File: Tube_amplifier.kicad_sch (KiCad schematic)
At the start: 3 parts, among them U1 6N2P, U2 6P14P

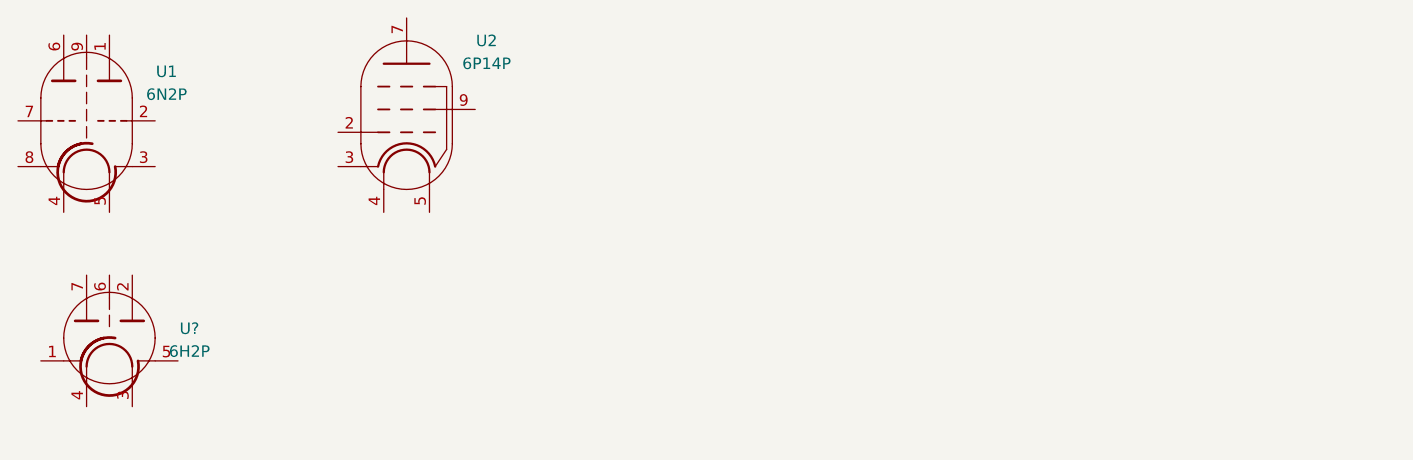
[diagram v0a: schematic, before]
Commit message: 7-pin socket 3d model added
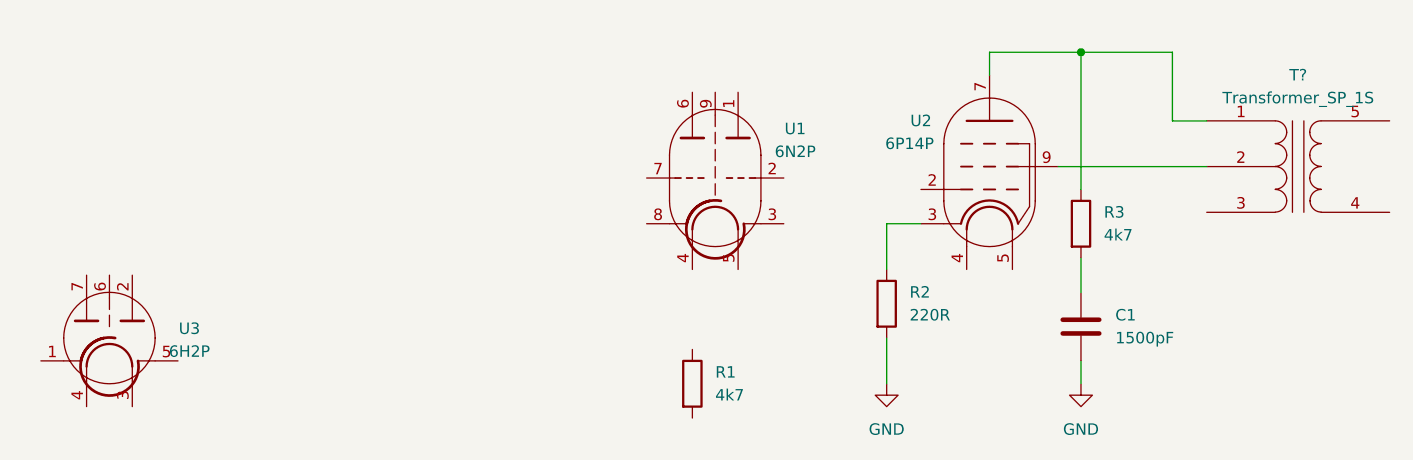
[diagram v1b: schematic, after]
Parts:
- added C1: 1500pF, Capacitor_THT:C_Rect_L7.2mm_W3.0mm_P5.00mm_FKS2_FKP2_MKS2_MKP2, symbol Device:C
- added R1: 4k7, spdf1626_lib:R_THT_025W, symbol Device:R
- added R2: 220R, spdf1626_lib:R_THT_1W, symbol Device:R
- added R3: 4k7, spdf1626_lib:R_THT_1W, symbol Device:R
- added T?: Transformer_SP_1S, symbol Device:Transformer_SP_1S
- gave numbers to parts that had none: 1
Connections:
- net at U2.3: now also R2.1
- net at U2.7: now also R3.1, T?.1 (PR1)
- net at U2.9: now also T?.2 (PM)
- new net: C1.1, R3.2
- new net GND: C1.2, R2.2
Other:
- moved on the sheet: U1, U2
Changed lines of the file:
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@@
 (kicad_sch (version 20211123) (generator eeschema)
   (paper "A4")
+  (junction (at 149.86 40.64) (diameter 0) (color 0 0 0 0)
+  )
+  (wire (pts (xy 147.32 53.34) (xy 163.83 53.34))
+    (stroke (width 0) (type default) (color 0 0 0 0))
+  )
+  (wire (pts (xy 149.86 40.64) (xy 139.7 40.64))
+    (stroke (width 0) (type default) (color 0 0 0 0))
+  )
+  (wire (pts (xy 160.02 48.26) (xy 160.02 40.64))
+    (stroke (width 0) (type default) (color 0 0 0 0))
+  )
+  (wire (pts (xy 139.7 40.64) (xy 139.7 43.18))
+    (stroke (width 0) (type default) (color 0 0 0 0))
+  )
+  (wire (pts (xy 128.27 64.77) (xy 128.27 59.69))
+    (stroke (width 0) (type default) (color 0 0 0 0))
+  )
+  (wire (pts (xy 149.86 55.88) (xy 149.86 40.64))
+    (stroke (width 0) (type default) (color 0 0 0 0))
+  )
+  (wire (pts (xy 163.83 48.26) (xy 160.02 48.26))
+    (stroke (width 0) (type default) (color 0 0 0 0))
+  )
+  (wire (pts (xy 128.27 72.39) (xy 128.27 77.47))
+    (stroke (width 0) (type default) (color 0 0 0 0))
+  )
+  (wire (pts (xy 149.86 63.5) (xy 149.86 67.31))
+    (stroke (width 0) (type default) (color 0 0 0 0))
+  )
+  (wire (pts (xy 128.27 59.69) (xy 132.08 59.69))
+    (stroke (width 0) (type default) (color 0 0 0 0))
+  )
+  (wire (pts (xy 160.02 40.64) (xy 149.86 40.64))
+    (stroke (width 0) (type default) (color 0 0 0 0))
+  )
+  (wire (pts (xy 149.86 74.93) (xy 149.86 77.47))
+    (stroke (width 0) (type default) (color 0 0 0 0))
+  )
+  (symbol (lib_id "power:GND") (at 128.27 77.47 0) (unit 1)
+    (in_bom yes) (on_board yes) (fields_autoplaced)
+    (property "Reference" "#PWR0101" (id 0) (at 128.27 83.82 0)
+      (effects (font (size 1.27 1.27)) hide)
+    )
+    (property "Value" "GND" (id 1) (at 128.27 82.55 0))
+    (property "Footprint" "" (id 2) (at 128.27 77.47 0)
+      (effects (font (size 1.27 1.27)) hide)
+    )
+    (property "Datasheet" "" (id 3) (at 128.27 77.47 0)
+      (effects (font (size 1.27 1.27)) hide)
+    )
+    (pin "1")
+  )
+  (symbol (lib_id "Device:R") (at 106.68 77.47 0) (unit 1)
+    (in_bom yes) (on_board yes) (fields_autoplaced)
+    (property "Reference" "R1" (id 0) (at 109.22 76.1999 0)
+      (effects (font (size 1.27 1.27)) (justify left))
+    )
+    (property "Value" "4k7" (id 1) (at 109.22 78.7399 0)
+      (effects (font (size 1.27 1.27)) (justify left))
+    )
+    (property "Footprint" "spdf1626_lib:R_THT_025W" (id 2) (at 104.902 77.47 90)
+      (effects (font (size 1.27 1.27)) hide)
+    )
+    (property "Datasheet" "~" (id 3) (at 106.68 77.47 0)
+      (effects (font (size 1.27 1.27)) hide)
+    )
+    (pin "1")
+    (pin "2")
+  )
+  (symbol (lib_id "Device:C") (at 149.86 71.12 0) (unit 1)
+    (in_bom yes) (on_board yes) (fields_autoplaced)
+    (property "Reference" "C1" (id 0) (at 153.67 69.8499 0)
+      (effects (font (size 1.27 1.27)) (justify left))
+    )
+    (property "Value" "1500pF" (id 1) (at 153.67 72.3899 0)
+      (effects (font (size 1.27 1.27)) (justify left))
+    )
+    (property "Footprint" "Capacitor_THT:C_Rect_L7.2mm_W3.0mm_P5.00mm_FKS2_FKP2_MKS2_MKP2" (id 2) (at 150.8252 74.93 0)
+      (effects (font (size 1.27 1.27)) hide)
+    )
+    (property "Datasheet" "~" (id 3) (at 149.86 71.12 0)
+      (effects (font (size 1.27 1.27)) hide)
+    )
+    (pin "1")
+    (pin "2")
+  )
+  (symbol (lib_id "Device:R") (at 128.27 68.58 0) (unit 1)
+    (in_bom yes) (on_board yes) (fields_autoplaced)
+    (property "Reference" "R2" (id 0) (at 130.81 67.3099 0)
+      (effects (font (size 1.27 1.27)) (justify left))
+    )
+    (property "Value" "220R" (id 1) (at 130.81 69.8499 0)
+      (effects (font (size 1.27 1.27)) (justify left))
+    )
+    (property "Footprint" "spdf1626_lib:R_THT_1W" (id 2) (at 126.492 68.58 90)
+      (effects (font (size 1.27 1.27)) hide)
+    )
+    (property "Datasheet" "~" (id 3) (at 128.27 68.58 0)
+      (effects (font (size 1.27 1.27)) hide)
+    )
+    (pin "1")
+    (pin "2")
+  )
+  (symbol (lib_id "power:GND") (at 149.86 77.47 0) (unit 1)
+    (in_bom yes) (on_board yes) (fields_autoplaced)
+    (property "Reference" "#PWR0102" (id 0) (at 149.86 83.82 0)
+      (effects (font (size 1.27 1.27)) hide)
+    )
+    (property "Value" "GND" (id 1) (at 149.86 82.55 0))
+    (property "Footprint" "" (id 2) (at 149.86 77.47 0)
+      (effects (font (size 1.27 1.27)) hide)
+    )
+    (property "Datasheet" "" (id 3) (at 149.86 77.47 0)
+      (effects (font (size 1.27 1.27)) hide)
+    )
+    (pin "1")
+  )
   (symbol (lib_id "spdf1626:6H2P") (at 41.91 72.39 0) (unit 1)
     (in_bom yes) (on_board yes) (fields_autoplaced)
-    (property "Reference" "U?" (id 0) (at 50.8 71.3486 0))
+    (property "Reference" "U3" (id 0) (at 50.8 71.3486 0))
     (property "Value" "6H2P" (id 1) (at 50.8 73.8886 0))
     (property "Footprint" "spdf1626_lib:9-pin_tube_socket" (id 2) (at 36.83 83.82 0)
@@
     (pin "7")
   )
-  (symbol (lib_id "spdf1626:6N2P") (at 39.37 48.26 0) (unit 1)
-    (in_bom yes) (on_board yes) (fields_autoplaced)
-    (property "Reference" "U1" (id 0) (at 48.26 42.7988 0))
-    (property "Value" "6N2P" (id 1) (at 48.26 45.3388 0))
-    (property "Footprint" "spdf1626_lib:9-pin_tube_socket" (id 2) (at 34.29 59.69 0)
-      (effects (font (size 1.27 1.27)) hide)
-    )
-    (property "Datasheet" "" (id 3) (at 39.37 50.8 0)
+  (symbol (lib_id "spdf1626:6N2P") (at 109.22 54.61 0) (unit 1)
+    (in_bom yes) (on_board yes) (fields_autoplaced)
+    (property "Reference" "U1" (id 0) (at 118.11 49.1488 0))
+    (property "Value" "6N2P" (id 1) (at 118.11 51.6888 0))
+    (property "Footprint" "spdf1626_lib:9-pin_tube_socket" (id 2) (at 104.14 66.04 0)
+      (effects (font (size 1.27 1.27)) hide)
+    )
+    (property "Datasheet" "" (id 3) (at 109.22 57.15 0)
       (effects (font (size 1.27 1.27)) hide)
     )
@@
     (pin "9")
   )
-  (symbol (lib_id "spdf1626:6P14P") (at 74.93 48.26 0) (unit 1)
+  (symbol (lib_id "Device:Transformer_SP_1S") (at 173.99 53.34 0) (unit 1)
+    (in_bom yes) (on_board yes) (fields_autoplaced)
+    (property "Reference" "T?" (id 0) (at 174.0027 43.18 0))
+    (property "Value" "Transformer_SP_1S" (id 1) (at 174.0027 45.72 0))
+    (property "Footprint" "" (id 2) (at 173.99 53.34 0)
+      (effects (font (size 1.27 1.27)) hide)
+    )
+    (property "Datasheet" "~" (id 3) (at 173.99 53.34 0)
+      (effects (font (size 1.27 1.27)) hide)
+    )
+    (pin "1")
+    (pin "2")
+    (pin "3")
+    (pin "4")
+    (pin "5")
+  )
+  (symbol (lib_id "spdf1626:6P14P") (at 139.7 54.61 0) (unit 1)
     (in_bom yes) (on_board yes)
-    (property "Reference" "U2" (id 0) (at 83.82 39.37 0))
-    (property "Value" "6P14P" (id 1) (at 83.82 41.91 0))
-    (property "Footprint" "spdf1626_lib:9-pin_tube_socket" (id 2) (at 69.85 59.69 0)
-      (effects (font (size 1.27 1.27)) hide)
-    )
-    (property "Datasheet" "" (id 3) (at 74.93 50.8 0)
+    (property "Reference" "U2" (id 0) (at 132.08 48.26 0))
+    (property "Value" "6P14P" (id 1) (at 130.81 50.8 0))
+    (property "Footprint" "spdf1626_lib:9-pin_tube_socket" (id 2) (at 134.62 66.04 0)
+      (effects (font (size 1.27 1.27)) hide)
+    )
+    (property "Datasheet" "" (id 3) (at 139.7 57.15 0)
       (effects (font (size 1.27 1.27)) hide)
     )
@@
     (pin "9")
   )
+  (symbol (lib_id "Device:R") (at 149.86 59.69 0) (unit 1)
+    (in_bom yes) (on_board yes) (fields_autoplaced)
+    (property "Reference" "R3" (id 0) (at 152.4 58.4199 0)
+      (effects (font (size 1.27 1.27)) (justify left))
+    )
+    (property "Value" "4k7" (id 1) (at 152.4 60.9599 0)
+      (effects (font (size 1.27 1.27)) (justify left))
+    )
+    (property "Footprint" "spdf1626_lib:R_THT_1W" (id 2) (at 148.082 59.69 90)
+      (effects (font (size 1.27 1.27)) hide)
+    )
+    (property "Datasheet" "~" (id 3) (at 149.86 59.69 0)
+      (effects (font (size 1.27 1.27)) hide)
+    )
+    (pin "1")
+    (pin "2")
+  )
   (sheet_instances
     (path "/" (page "1"))
   )
   (symbol_instances
+    (path "/174e99dc-92b2-4f3c-b711-6020058d5916"
+      (reference "#PWR0101") (unit 1) (value "GND") (footprint "")
+    )
+    (path "/ab444bc9-d57b-4747-8ef6-d78764df7a8c"
+      (reference "#PWR0102") (unit 1) (value "GND") (footprint "")
+    )
+    (path "/8020425b-e9f3-495c-818a-7f5fd22a8d70"
+      (reference "C1") (unit 1) (value "1500pF") (footprint "Capacitor_THT:C_Rect_L7.2mm_W3.0mm_P5.00mm_FKS2_FKP2_MKS2_MKP2")
+    )
+    (path "/44eb7b55-8f82-421f-960a-57dc31a92d41"
+      (reference "R1") (unit 1) (value "4k7") (footprint "spdf1626_lib:R_THT_025W")
+    )
+    (path "/9d8d7bde-1411-4ced-8a1f-3f0a14f213bb"
+      (reference "R2") (unit 1) (value "220R") (footprint "spdf1626_lib:R_THT_1W")
+    )
+    (path "/f80a85fd-e6d4-41d6-ba9f-12f575651e85"
+      (reference "R3") (unit 1) (value "4k7") (footprint "spdf1626_lib:R_THT_1W")
+    )
+    (path "/d9a9c68a-47eb-46dd-b222-1db384ecbe9f"
+      (reference "T?") (unit 1) (value "Transformer_SP_1S") (footprint "")
+    )
     (path "/ce74a986-7574-4a88-aecc-2859912e2c22"
       (reference "U1") (unit 1) (value "6N2P") (footprint "spdf1626_lib:9-pin_tube_socket")
@@
     )
     (path "/bafa2160-6973-4a93-a628-776a08d6455e"
-      (reference "U?") (unit 1) (value "6H2P") (footprint "spdf1626_lib:9-pin_tube_socket")
-    )
-  )
+      (reference "U3") (unit 1) (value "6H2P") (footprint "spdf1626_lib:9-pin_tube_socket")
+    )
+  )

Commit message: Main part of schematic done
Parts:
- added C?: 0,033uF, Capacitor_THT:C_Rect_L7.2mm_W3.0mm_P5.00mm_FKS2_FKP2_MKS2_MKP2, symbol Device:C
- added C? (x3): 2200pF, Capacitor_THT:C_Rect_L7.2mm_W3.0mm_P5.00mm_FKS2_FKP2_MKS2_MKP2, symbol Device:C
- added C?: 0,047uF, Capacitor_THT:C_Rect_L7.2mm_W3.0mm_P5.00mm_FKS2_FKP2_MKS2_MKP2, symbol Device:C
- added C?: 3300pF, Capacitor_THT:C_Rect_L7.2mm_W3.0mm_P5.00mm_FKS2_FKP2_MKS2_MKP2, symbol Device:C
- added C?: 27pF, Capacitor_THT:C_Rect_L7.2mm_W3.0mm_P5.00mm_FKS2_FKP2_MKS2_MKP2, symbol Device:C
- added C?: 5,6pF, Capacitor_THT:C_Rect_L7.2mm_W3.0mm_P5.00mm_FKS2_FKP2_MKS2_MKP2, symbol Device:C
- added C?: 0,01uF, Capacitor_THT:C_Rect_L7.2mm_W3.0mm_P5.00mm_FKS2_FKP2_MKS2_MKP2, symbol Device:C
- added C?: 4700pF, Capacitor_THT:C_Rect_L7.2mm_W3.0mm_P5.00mm_FKS2_FKP2_MKS2_MKP2, symbol Device:C
- added J?: AudioJack3, symbol Connector:AudioJack3
- added R?: 6k8, spdf1626_lib:R_THT_025W, symbol Device:R
- added R?: 33k, spdf1626_lib:R_THT_025W, symbol Device:R
- added R?: 120k, spdf1626_lib:R_THT_025W, symbol Device:R
- added R? (x3): 220k, spdf1626_lib:R_THT_025W, symbol Device:R
- added R?: 2k7, spdf1626_lib:R_THT_025W, symbol Device:R
- added R?: 3k3, spdf1626_lib:R_THT_025W, symbol Device:R
- added R?: 51k, spdf1626_lib:R_THT_025W, symbol Device:R
- added RV?: 470k, symbol Device:R_Potentiometer
- added RV?: 2,2M, symbol Device:R_Potentiometer
- added RV?: 1M, symbol Device:R_Potentiometer
- R1: value 4k7 -> 6k8
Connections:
- net GND: now also T?.4 (S1), U1.5, U2.5, C?.2, C?.2, R?.1, R?.1, R?.1, R?.1, RV?.1
- net at R1.1: now also C?.2, R?.2
- net at R1.2: now also U2.2
- net at U1.1: now also C?.1, C?.2, R?.1
- net at U1.2: now also RV?.2
- net at U1.3: now also C?.1, C?.2, R?.2, R?.2
- net +6V: now reaches U1.4
- net +6V: now also U2.4
- net at U1.6: now also C?.2, R?.1
- net at U1.7: now also C?.2, RV?.2
- net at U1.8: now also C?.1, R?.2
- net 240V: now reaches T?.3 (PR2)
- net 240V: now also R?.2, R?.2
- net Left_output: now reaches T?.5 (S2)
- net Left_output: now also R?.1
- new net: C?.1, C?.1, R?.2
- new net: C?.1, C?.2, RV?.3
- new net: C?.1, R?.1, RV?.1
- new net: C?.1, C?.2, R?.2, RV?.2
- new net: R?.1, RV?.3
- new net: C?.2, R?.2, RV?.1
- new net: C?.1, RV?.3
- new net Left_input: C?.1
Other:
- moved on the sheet: R1, U1, U3

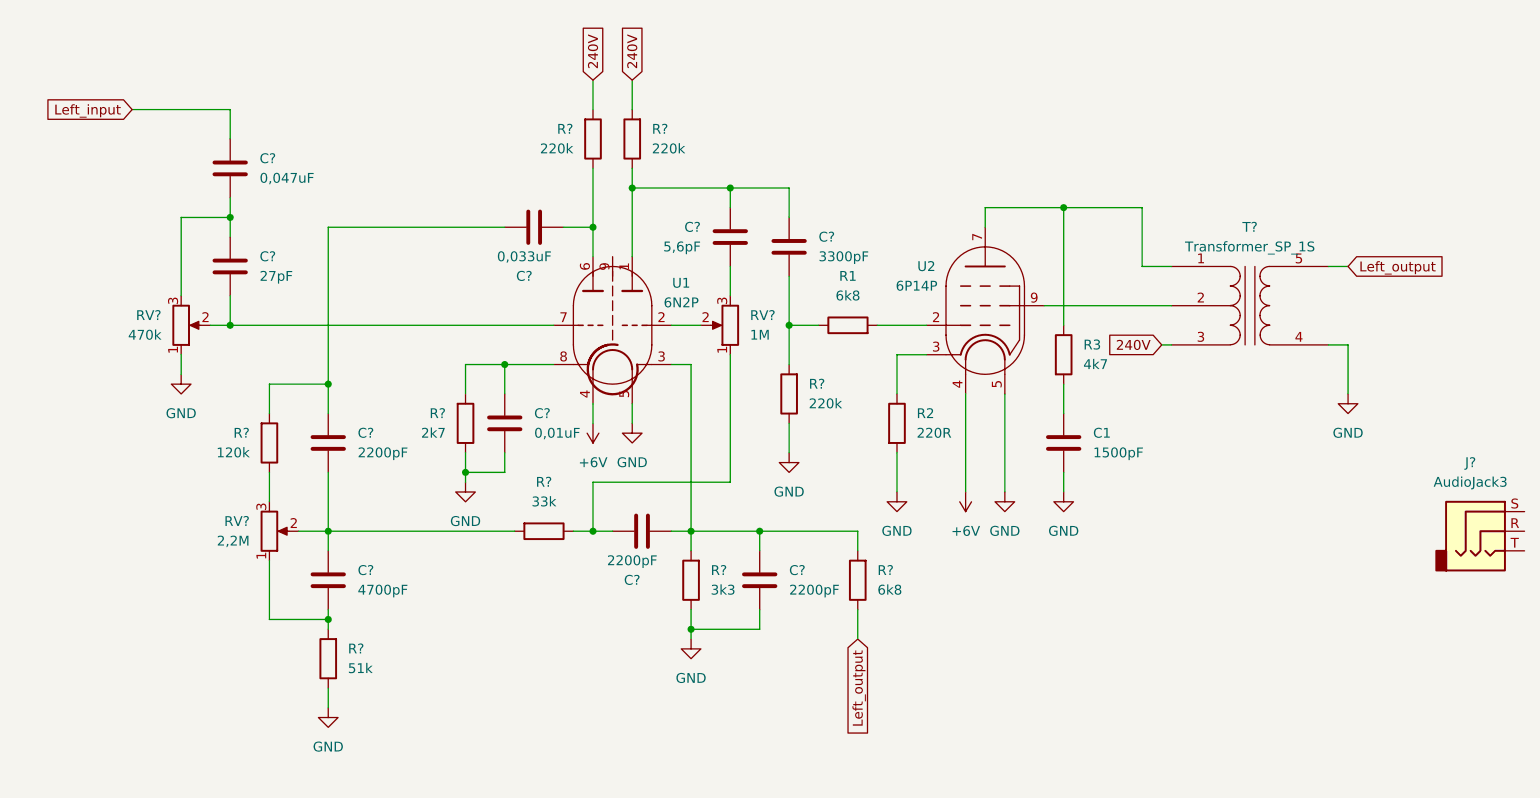
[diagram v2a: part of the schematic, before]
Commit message: Output transformer added, pcb v0.1 ready
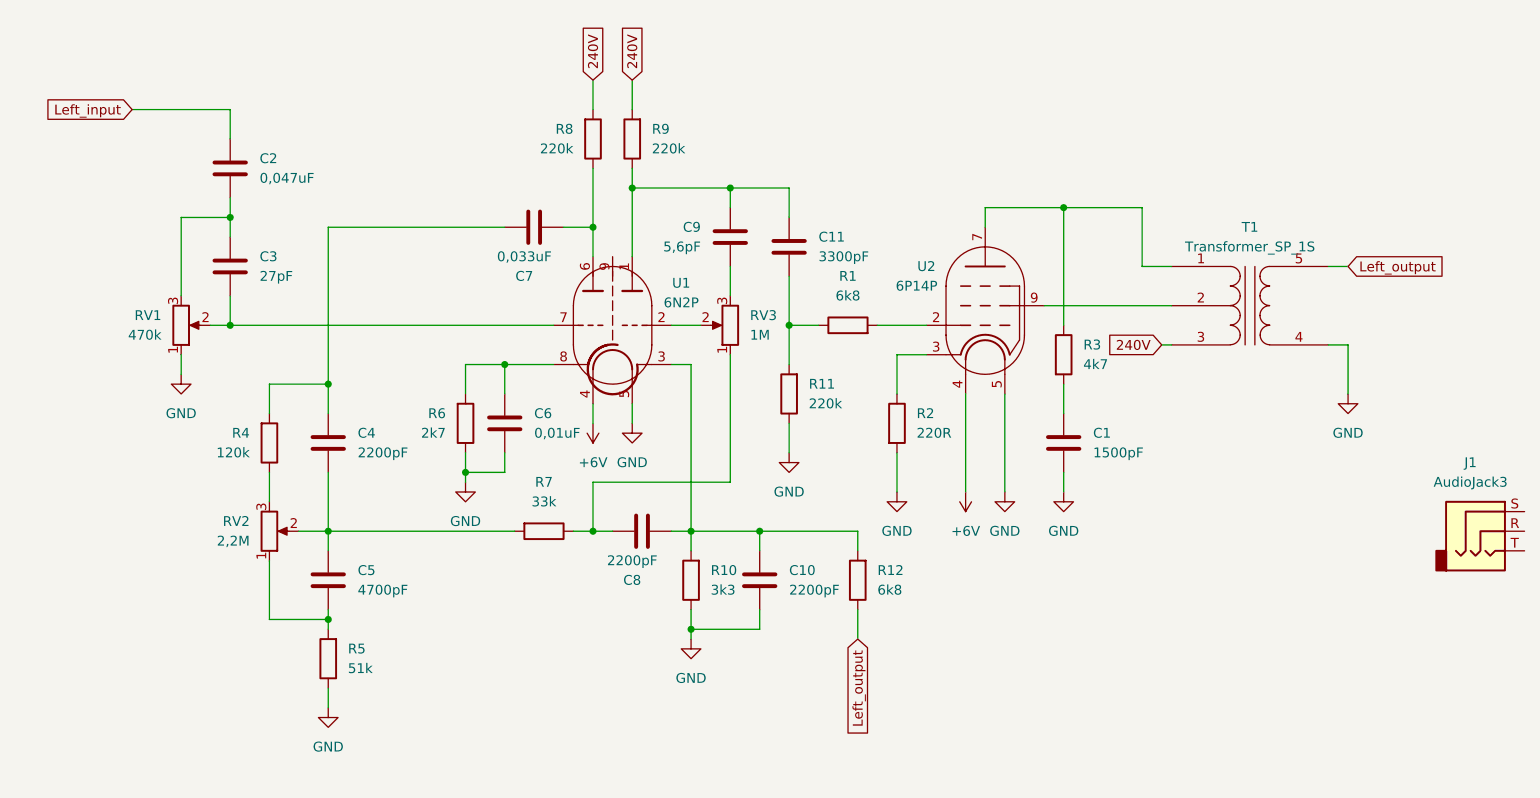
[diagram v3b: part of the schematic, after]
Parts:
- C1: footprint Capacitor_THT:C_Rect_L7.2mm_W3.0mm_P5.00mm_FKS2_FKP2_MKS2_MKP2 -> spdf1626_lib:C_THT_K73-17_P5.00mm
- C10, C11, C2, C3, C4, C5, C6, C7, C9: renamed from C?; footprint Capacitor_THT:C_Rect_L7.2mm_W3.0mm_P5.00mm_FKS2_FKP2_MKS2_MKP2 -> spdf1626_lib:C_THT_K73-17_P5.00mm
- T1: renamed from T?; footprint (none) -> spdf1626_lib:Output_transformer
- gave numbers to parts that had none: 14

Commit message: 7-pin tube socket added
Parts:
- U3: footprint spdf1626_lib:9-pin_tube_socket -> spdf1626_lib:7-pin_tube_socket
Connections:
- net GND: now also U1.9
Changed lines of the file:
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@@
+    (stroke (width 0) (type default) (color 0 0 0 0))
+  )
+  (wire (pts (xy 91.44 40.64) (xy 91.44 46.99))
     (stroke (width 0) (type default) (color 0 0 0 0))
   )
@@
     (pin "3")
   )
+  (symbol (lib_id "power:GND") (at 91.44 40.64 180) (unit 1)
+    (in_bom yes) (on_board yes) (fields_autoplaced)
+    (property "Reference" "#PWR?" (id 0) (at 91.44 34.29 0)
+      (effects (font (size 1.27 1.27)) hide)
+    )
+    (property "Value" "GND" (id 1) (at 93.98 39.3699 0)
+      (effects (font (size 1.27 1.27)) (justify right))
+    )
+    (property "Footprint" "" (id 2) (at 91.44 40.64 0)
+      (effects (font (size 1.27 1.27)) hide)
+    )
+    (property "Datasheet" "" (id 3) (at 91.44 40.64 0)
+      (effects (font (size 1.27 1.27)) hide)
+    )
+    (pin "1")
+  )
   (symbol (lib_id "power:GND") (at 93.98 68.58 0) (unit 1)
     (in_bom yes) (on_board yes) (fields_autoplaced)
@@
     (property "Reference" "U3" (id 0) (at 68.58 138.6586 0))
     (property "Value" "6H2P" (id 1) (at 68.58 141.1986 0))
-    (property "Footprint" "spdf1626_lib:9-pin_tube_socket" (id 2) (at 54.61 151.13 0)
+    (property "Footprint" "spdf1626_lib:7-pin_tube_socket" (id 2) (at 54.61 151.13 0)
       (effects (font (size 1.27 1.27)) hide)
     )
@@
       (reference "#PWR0102") (unit 1) (value "GND") (footprint "")
     )
+    (path "/7915db52-1f07-44c7-b796-c7fc1aca7b67"
+      (reference "#PWR?") (unit 1) (value "GND") (footprint "")
+    )
     (path "/8020425b-e9f3-495c-818a-7f5fd22a8d70"
       (reference "C1") (unit 1) (value "1500pF") (footprint "spdf1626_lib:C_THT_K73-17_P5.00mm")
@@
     )
     (path "/bafa2160-6973-4a93-a628-776a08d6455e"
-      (reference "U3") (unit 1) (value "6H2P") (footprint "spdf1626_lib:9-pin_tube_socket")
-    )
-  )
+      (reference "U3") (unit 1) (value "6H2P") (footprint "spdf1626_lib:7-pin_tube_socket")
+    )
+  )
